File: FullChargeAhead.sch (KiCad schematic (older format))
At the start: 18 parts, among them P101 USB_OTG, P102 CONN_01X02, P103 JST_2PIN, P104 CONN_01X02, P105 CONN_01X02, U101 MCP73834

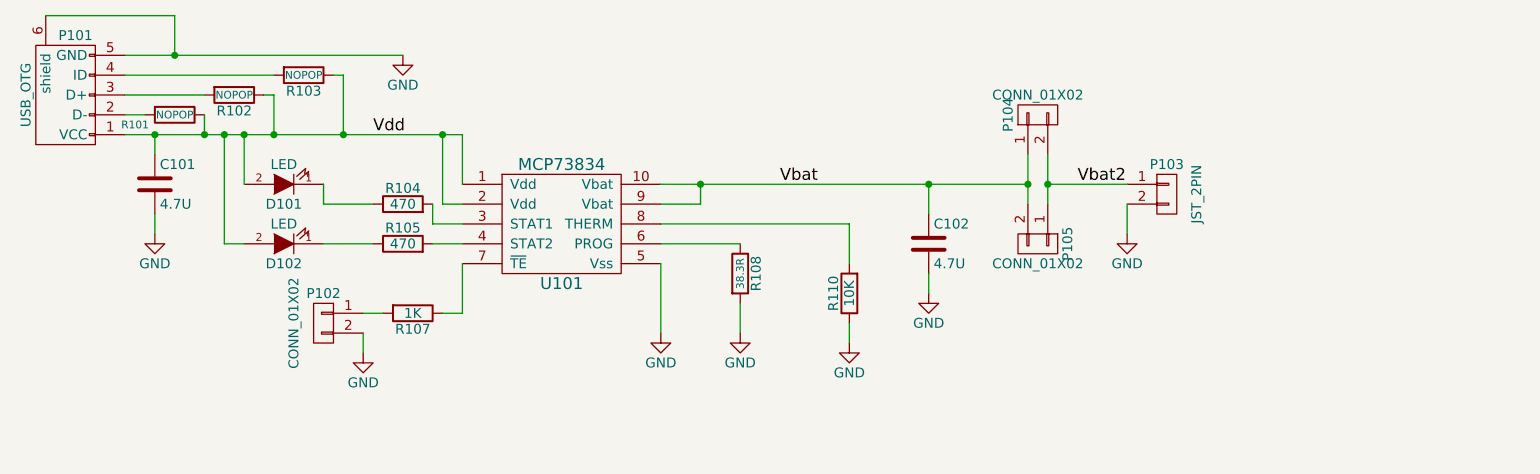
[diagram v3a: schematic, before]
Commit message: initial board layout and copper fills
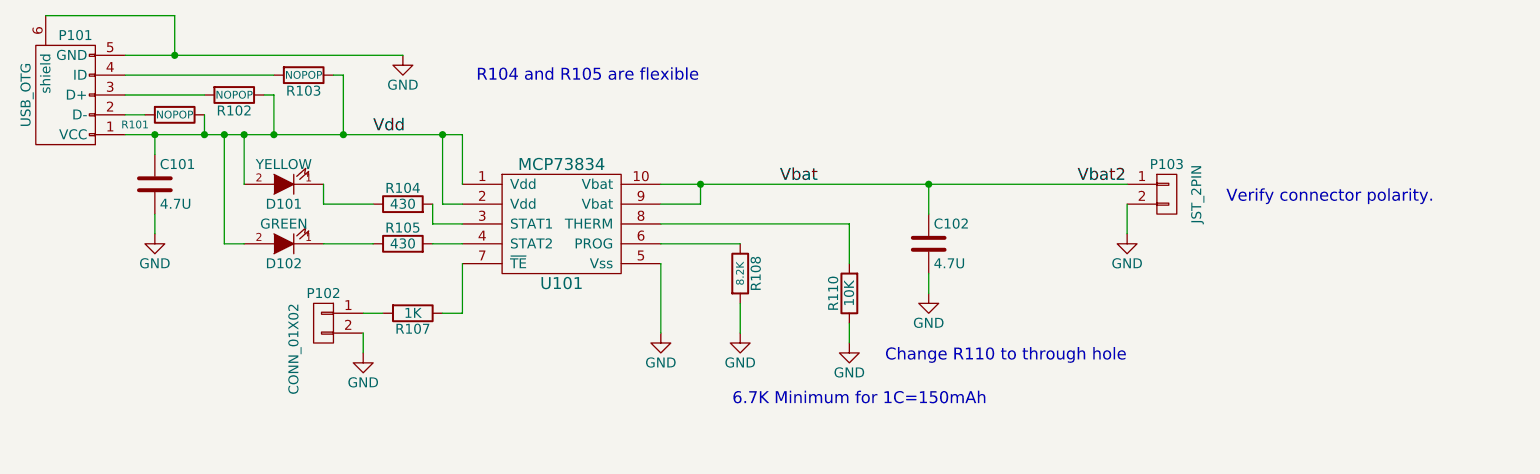
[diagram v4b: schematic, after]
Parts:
- removed P104: CONN_01X02, Pin_Headers:Pin_Header_Straight_1x02, symbol CONN_01X02
- removed P105: CONN_01X02, FullChargeAhead:Terminal_Block_200_mil, symbol CONN_01X02
- C101, C102: footprint Capacitors_SMD:C_1206_HandSoldering -> Capacitors_SMD:C_0805_HandSoldering
- D101: value LED -> YELLOW; MPN (none) -> LTST-C171KSKT
- D102: value LED -> GREEN; MPN (none) -> LTST-C171GKT
- P101: Fieldname Value -> (none)
- P102: Fieldname (none) -> Value; MPN S2B-PH-K-S(LF)(SN) -> (none)
- R104, R105: value 470 -> 430
- R108: value 38.3R -> 8.2K
- R110: footprint Resistors_SMD:R_0805_HandSoldering -> Resistors_ThroughHole:Resistor_Horizontal_RM10mm
- U101: Datasheet (none) -> http://ww1.microchip.com/downloads/en/DeviceDoc/22005b.pdf; Fieldname Value -> (none)
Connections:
- net Vbat2 is gone; now on net Vbat: P103.1 (P1)
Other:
- note added: "6.7K Minimum for 1C=150mAh"
- note added: "Change R110 to through hole"
- note added: "R104 and R105 are flexible"
- note added: "Verify connector polarity."
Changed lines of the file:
@@
 Rev ""
 Comp ""
-Comment1 "Note 1: R107 must be sized to match max charge rate of battery. 38.3K = 110mA at 4.2V"
+Comment1 "Note 1: R108 must be sized to match max charge rate of battery. 8.2K = 122mA at 4.2V"
 Comment2 "Note 2: Verify polarity of connection P103 matches polarity of battery connector"
 Comment3 ""
@@
 F 2 "Housings_SSOP:MSOP-10_3x3mm_Pitch0.5mm" H 5500 3350 60  0001 C CNN
 F 3 "http://ww1.microchip.com/downloads/en/DeviceDoc/22005b.pdf" H 5500 3350 60  0001 C CNN
-F 4 "Value" H 5500 3350 60  0001 C CNN "Fieldname"
+F 4 "http://ww1.microchip.com/downloads/en/DeviceDoc/22005b.pdf" H 5500 3350 60  0001 C CNN "Datasheet"
 F 5 "MCP73834-FCI/UN" H 5500 3350 60  0001 C CNN "MPN"
 	1    5500 3350
@@
 P 6400 3600
 F 0 "R108" V 6480 3600 50  0000 C CNN
-F 1 "38.3R" V 6400 3600 39  0000 C CNN
+F 1 "8.2K" V 6400 3600 39  0000 C CNN
 F 2 "Resistors_SMD:R_0805_HandSoldering" V 6330 3600 50  0001 C CNN
 F 3 "" H 6400 3600 50  0000 C CNN
@@
 P 4700 3450
 F 0 "R105" V 4780 3450 50  0000 C CNN
-F 1 "470" V 4700 3450 50  0000 C CNN
+F 1 "430" V 4700 3450 50  0000 C CNN
 F 2 "Resistors_SMD:R_0805_HandSoldering" V 4630 3450 50  0001 C CNN
 F 3 "" H 4700 3450 50  0000 C CNN
@@
 P 4700 3250
 F 0 "R104" V 4780 3250 50  0000 C CNN
-F 1 "470" V 4700 3250 50  0000 C CNN
+F 1 "430" V 4700 3250 50  0000 C CNN
 F 2 "Resistors_SMD:R_0805_HandSoldering" V 4630 3250 50  0001 C CNN
 F 3 "" H 4700 3250 50  0000 C CNN
@@
 F 0 "C102" H 7375 3550 50  0000 L CNN
 F 1 "4.7U" H 7375 3350 50  0000 L CNN
-F 2 "Capacitors_SMD:C_1206_HandSoldering" H 7388 3300 50  0001 C CNN
+F 2 "Capacitors_SMD:C_0805_HandSoldering" H 7388 3300 50  0001 C CNN
 F 3 "" H 7350 3450 50  0000 C CNN
 	1    7350 3450
@@
 P 4100 3450
 F 0 "D102" H 4100 3550 50  0000 C CNN
-F 1 "LED" H 4100 3350 50  0000 C CNN
+F 1 "GREEN" H 4100 3350 50  0000 C CNN
 F 2 "LEDs:LED_0805" H 4100 3450 50  0001 C CNN
 F 3 "" H 4100 3450 50  0000 C CNN
+F 4 "LTST-C171GKT" H 4100 3450 60  0001 C CNN "MPN"
 	1    4100 3450
 	-1   0    0    1
@@
 P 4100 3150
 F 0 "D101" H 4100 3250 50  0000 C CNN
-F 1 "LED" H 4100 3050 50  0000 C CNN
+F 1 "YELLOW" H 4100 3050 50  0000 C CNN
 F 2 "LEDs:LED_0805" H 4100 3150 50  0001 C CNN
 F 3 "" H 4100 3150 50  0000 C CNN
+F 4 "LTST-C171KSKT" H 4100 3150 60  0001 C CNN "MPN"
 	1    4100 3150
 	-1   0    0    1
@@
 F 0 "C101" H 3475 3250 50  0000 L CNN
 F 1 "4.7U" H 3475 3050 50  0000 L CNN
-F 2 "Capacitors_SMD:C_1206_HandSoldering" H 3488 3000 50  0001 C CNN
+F 2 "Capacitors_SMD:C_0805_HandSoldering" H 3488 3000 50  0001 C CNN
 F 3 "" H 3450 3150 50  0000 C CNN
 	1    3450 3150
@@
 F 2 "FullChargeAhead:USB_Micro-B_10103594-0001LF" V 2950 2600 50  0001 C CNN
 F 3 "http://portal.fciconnect.com/Comergent//fci/drawing/10103594.pdf" V 2950 2600 50  0001 C CNN
-F 4 "Value" H 3000 2700 60  0001 C CNN "Fieldname"
-F 5 "10103594-0001LF" H 3000 2700 60  0001 C CNN "MPN"
+F 4 "10103594-0001LF" H 3000 2700 60  0001 C CNN "MPN"
 	1    3000 2700
 	0    -1   -1   0
@@
 P 4300 3850
 F 0 "P102" H 4300 4000 50  0000 C CNN
-F 1 "CONN_01X02" V 4450 3850 50  0000 C CNN
+F 1 "CONN_01X02" V 4450 3720 50  0000 C CNN
 F 2 "Pin_Headers:Pin_Header_Straight_1x02" H 4300 3850 50  0001 C CNN
-F 3 "http://www.jst-mfg.com/product/pdf/eng/ePH.pdf" H 4300 3850 50  0001 C CNN
-F 4 "S2B-PH-K-S(LF)(SN)" H 4300 3850 60  0001 C CNN "MPN"
+F 3 "" H 4300 3850 50  0001 C CNN
+F 4 "Value" H 4300 3850 60  0001 C CNN "Fieldname"
 	1    4300 3850
 	-1   0    0    -1
@@
 F 0 "R110" V 7030 3700 50  0000 C CNN
 F 1 "10K" V 6950 3700 50  0000 C CNN
-F 2 "Resistors_SMD:R_0805_HandSoldering" V 6880 3700 50  0001 C CNN
+F 2 "Resistors_ThroughHole:Resistor_Horizontal_RM10mm" V 6880 3700 50  0001 C CNN
 F 3 "" H 6950 3700 50  0000 C CNN
 	1    6950 3700
@@
 Wire Wire Line
 	6950 3350 6950 3550
-$Comp
-L CONN_01X02 P104
-U 1 1 57E203B6
-P 7900 2800
-F 0 "P104" H 7900 2950 50  0000 C CNN
-F 1 "CONN_01X02" V 8000 2800 50  0000 C CNN
-F 2 "Pin_Headers:Pin_Header_Straight_1x02" H 7900 2800 50  0001 C CNN
-F 3 "" H 7900 2800 50  0000 C CNN
-	1    7900 2800
-	0    -1   -1   0
-$EndComp
-$Comp
-L CONN_01X02 P105
-U 1 1 57E20401
-P 7900 3450
-F 0 "P105" H 7900 3600 50  0000 C CNN
-F 1 "CONN_01X02" V 8000 3450 50  0000 C CNN
-F 2 "FullChargeAhead:Terminal_Block_200_mil" H 7900 3450 50  0001 C CNN
-F 3 "" H 7900 3450 50  0000 C CNN
-F 4 "OSTTC022162" H 7900 3450 60  0001 C CNN "MPN"
-	1    7900 3450
-	0    1    1    0
-$EndComp
-Wire Wire Line
-	6000 3150 7850 3150
-Wire Wire Line
-	7850 3000 7850 3250
+Wire Wire Line
+	6000 3150 8350 3150
 Wire Wire Line
 	7350 3300 7350 3150
@@
 	6200 3250 6200 3150
 Connection ~ 6200 3150
-Connection ~ 7850 3150
-Wire Wire Line
-	7950 3000 7950 3250
-Wire Wire Line
-	8350 3150 7950 3150
-Connection ~ 7950 3150
 Text Label 6600 3150 0    60   ~ 0
 Vbat
 Text Label 8100 3150 0    60   ~ 0
 Vbat2
+Text Notes 5070 2640 0    60   ~ 0
+R104 and R105 are flexible
+Text Notes 7130 4050 0    60   ~ 0
+Change R110 to through hole
+Text Notes 8850 3250 0    60   ~ 0
+Verify connector polarity.
+Text Notes 6360 4270 0    60   ~ 0
+6.7K Minimum for 1C=150mAh
 $EndSCHEMATC

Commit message: new usb connector, via stiching, and gerbers
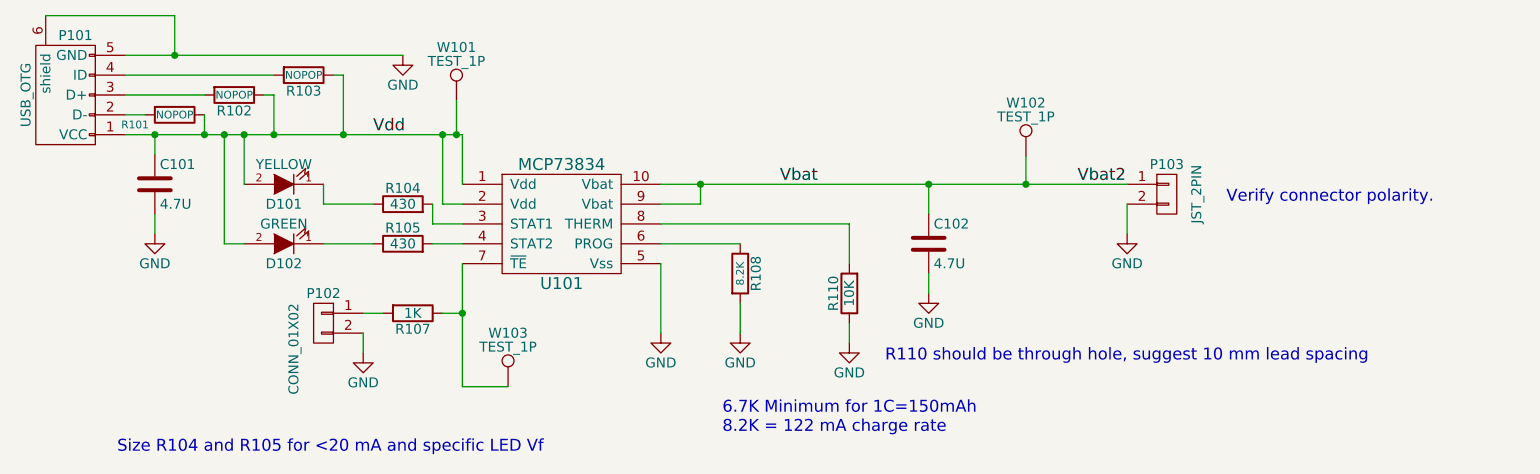
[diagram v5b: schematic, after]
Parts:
- added W101, W102, W103: TEST_1P, Measurement_Points:Measurement_Point_Round-SMD-Pad_Small, symbol TEST_1P
- P101: footprint FullChargeAhead:USB_Micro-B_10103594-0001LF -> FullChargeAhead:10118193; Fieldname (none) -> Value; MPN 10103594-0001LF -> 10118193-0001LF
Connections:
- net Vbat: now also W102.1
- net Vdd: now also W101.1
- net at R107.1, U101.7 (~TE): now also W103.1
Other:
- note added: "6.7K Minimum for 1C=150mAh\n8.2K = 122 mA charge rate"
- note added: "R110 should be through hole, suggest 10 mm lead spacing"
- note added: "Size R104 and R105 for <20 mA and specific LED Vf"
- note removed: "6.7K Minimum for 1C=150mAh"
- note removed: "Change R110 to through hole"
- note removed: "R104 and R105 are flexible"
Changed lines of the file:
@@
 F 0 "P101" V 3300 2650 50  0000 C CNN
 F 1 "USB_OTG" H 3000 2900 50  0000 C CNN
-F 2 "FullChargeAhead:USB_Micro-B_10103594-0001LF" V 2950 2600 50  0001 C CNN
-F 3 "http://portal.fciconnect.com/Comergent//fci/drawing/10103594.pdf" V 2950 2600 50  0001 C CNN
-F 4 "10103594-0001LF" H 3000 2700 60  0001 C CNN "MPN"
+F 2 "FullChargeAhead:10118193" V 2950 2600 50  0001 C CNN
+F 3 "http://portal.fciconnect.com/Comergent//fci/drawing/10118193.pdf" V 2950 2600 50  0001 C CNN
+F 4 "Value" H 3000 2700 60  0001 C CNN "Fieldname"
+F 5 "10118193-0001LF" H 3000 2700 60  0001 C CNN "MPN"
 	1    3000 2700
 	0    -1   -1   0
@@
 $EndComp
 Wire Wire Line
-	5000 3550 5000 3800
+	5000 3550 5000 4170
 Wire Wire Line
 	5000 3800 4900 3800
@@
 Text Label 8100 3150 0    60   ~ 0
 Vbat2
-Text Notes 5070 2640 0    60   ~ 0
-R104 and R105 are flexible
+Text Notes 3260 4510 0    60   ~ 0
+Size R104 and R105 for <20 mA and specific LED Vf
 Text Notes 7130 4050 0    60   ~ 0
-Change R110 to through hole
+R110 should be through hole, suggest 10 mm lead spacing
 Text Notes 8850 3250 0    60   ~ 0
 Verify connector polarity.
-Text Notes 6360 4270 0    60   ~ 0
-6.7K Minimum for 1C=150mAh
+Text Notes 6310 4410 0    60   ~ 0
+6.7K Minimum for 1C=150mAh\n8.2K = 122 mA charge rate
+$Comp
+L TEST_1P W102
+U 1 1 5807C88C
+P 7840 3010
+F 0 "W102" H 7840 3280 50  0000 C CNN
+F 1 "TEST_1P" H 7840 3210 50  0000 C CNN
+F 2 "Measurement_Points:Measurement_Point_Round-SMD-Pad_Small" H 8040 3010 50  0001 C CNN
+F 3 "" H 8040 3010 50  0000 C CNN
+	1    7840 3010
+	1    0    0    -1
+$EndComp
+Wire Wire Line
+	7840 3010 7840 3150
+Connection ~ 7840 3150
+$Comp
+L TEST_1P W101
+U 1 1 5807CB7C
+P 4970 2730
+F 0 "W101" H 4970 3000 50  0000 C CNN
+F 1 "TEST_1P" H 4970 2930 50  0000 C CNN
+F 2 "Measurement_Points:Measurement_Point_Round-SMD-Pad_Small" H 5170 2730 50  0001 C CNN
+F 3 "" H 5170 2730 50  0000 C CNN
+	1    4970 2730
+	1    0    0    -1
+$EndComp
+Wire Wire Line
+	4970 2730 4970 2900
+Connection ~ 4970 2900
+$Comp
+L TEST_1P W103
+U 1 1 580DFE0E
+P 5230 4170
+F 0 "W103" H 5230 4440 50  0000 C CNN
+F 1 "TEST_1P" H 5230 4370 50  0000 C CNN
+F 2 "Measurement_Points:Measurement_Point_Round-SMD-Pad_Small" H 5430 4170 50  0001 C CNN
+F 3 "" H 5430 4170 50  0000 C CNN
+	1    5230 4170
+	1    0    0    -1
+$EndComp
+Wire Wire Line
+	5000 4170 5230 4170
+Connection ~ 5000 3800
 $EndSCHEMATC
